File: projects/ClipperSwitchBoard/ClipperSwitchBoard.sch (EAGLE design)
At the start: 8 parts

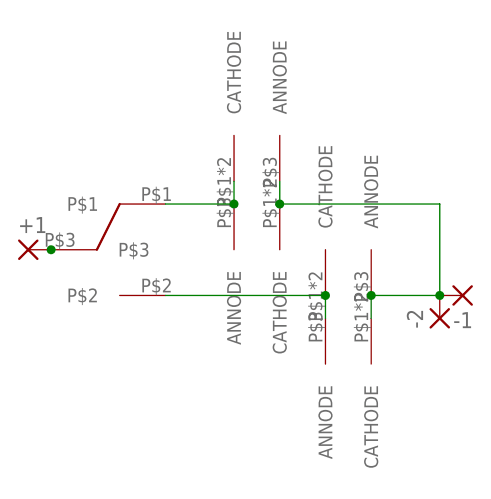
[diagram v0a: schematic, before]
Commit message: Updated to use new clipper block.
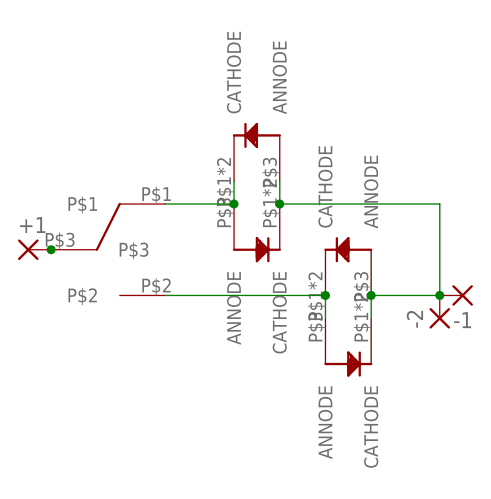
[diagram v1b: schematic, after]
